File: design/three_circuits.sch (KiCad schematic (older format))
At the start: 0 parts

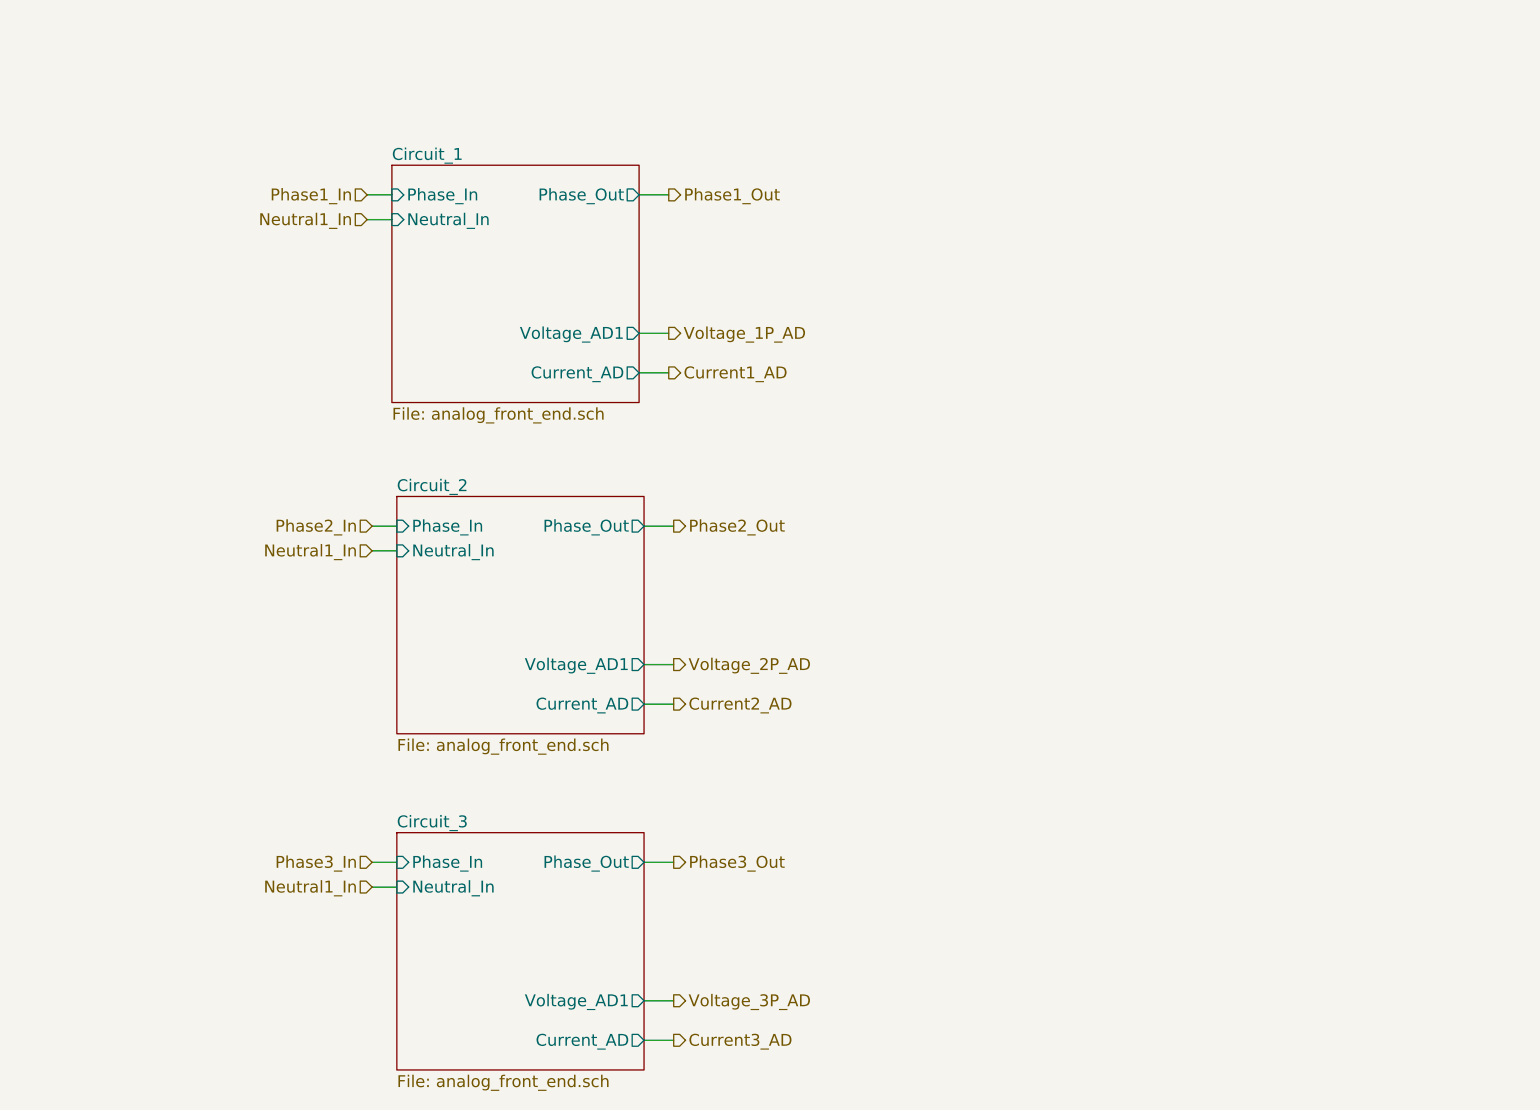
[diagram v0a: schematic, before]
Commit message: Moving to PIVI 2.0, added circuits for current clamps
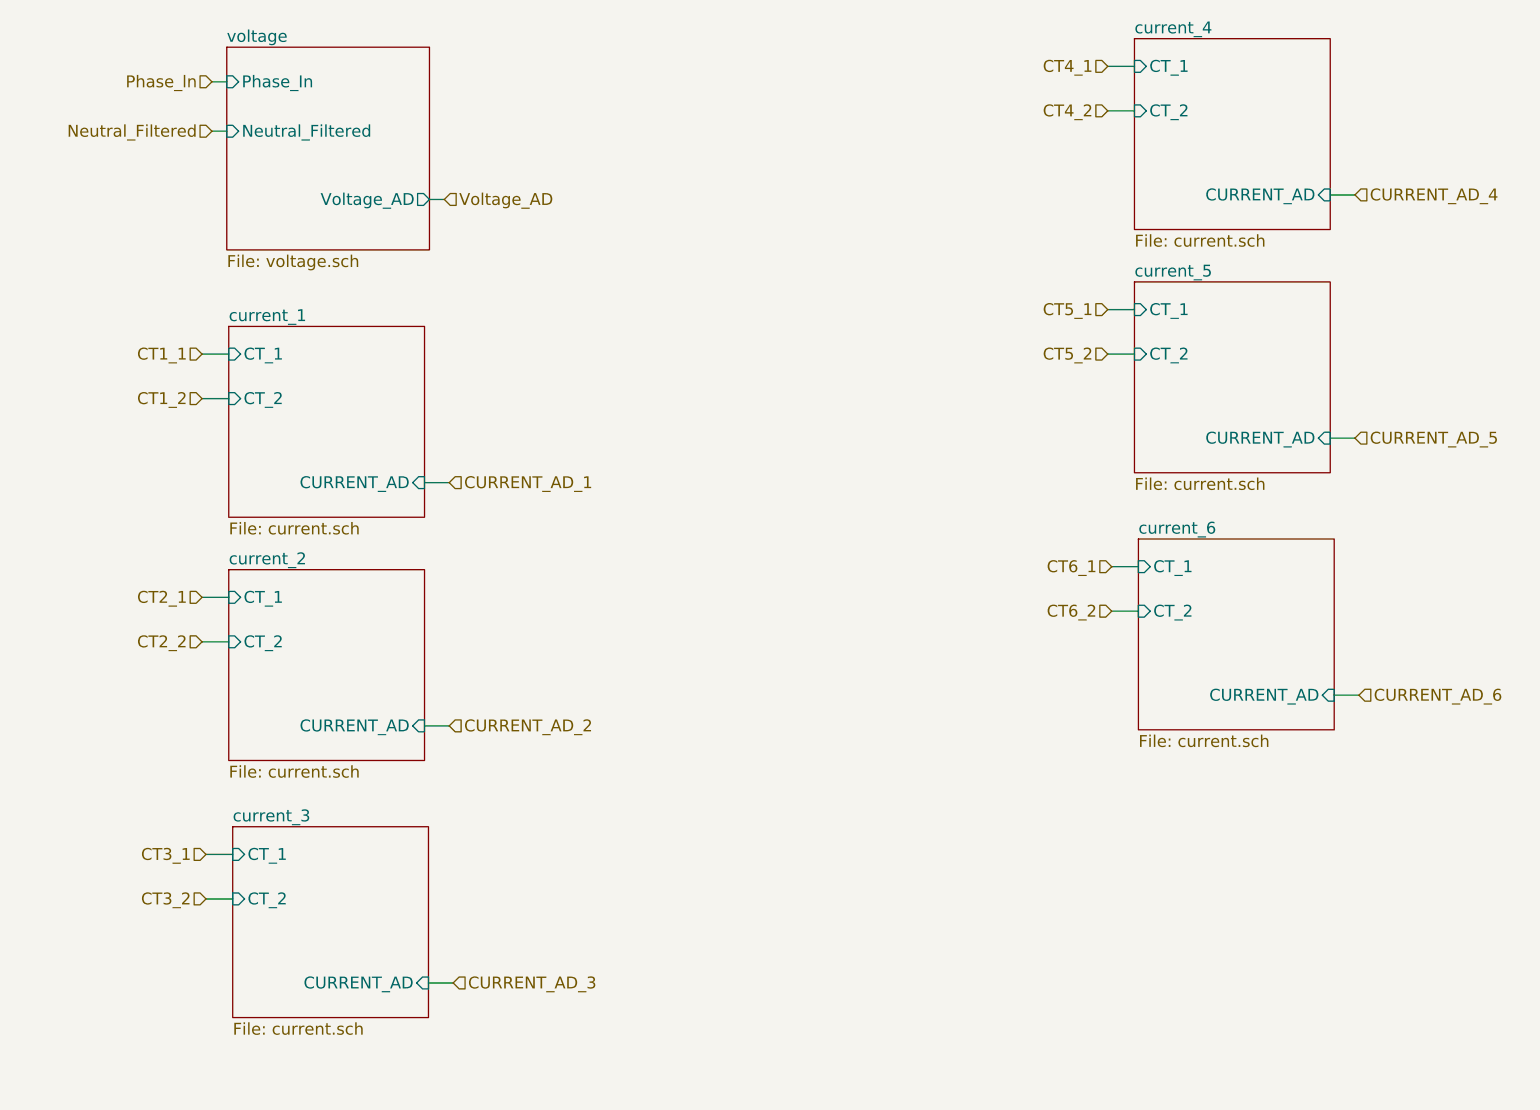
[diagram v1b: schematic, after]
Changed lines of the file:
@@
 LIBS:txs0104e
 LIBS:less
+LIBS:pivi-shield-cache
 EELAYER 25 0
 EELAYER END
 $Descr A4 11693 8268
 encoding utf-8
-Sheet 4 12
+Sheet 11 18
 Title "PIVI"
-Date ""
-Rev "1.0"
+Date "Mon 27 Jul 2015"
+Rev "2.0"
 Comp "Copyright (C) LESS industries S.A. 2014,2015"
 Comment1 "Share alike attribution non-commercial 4.0"
@@
 $EndDescr
 $Sheet
-S 2600 1500 1250 1200
-U 548E1940
-F0 "Circuit_1" 60
-F1 "analog_front_end.sch" 60
-F2 "Voltage_AD1" O R 3850 2350 60
-F3 "Phase_In" I L 2600 1650 60
-F4 "Phase_Out" O R 3850 1650 60
-F5 "Current_AD" O R 3850 2550 60
-F6 "Neutral_In" I L 2600 1775 60
+S 1765 903  1025 1025
+U 55B216B6
+F0 "voltage" 60
+F1 "voltage.sch" 60
+F2 "Phase_In" I L 1765 1078 60
+F3 "Voltage_AD" O R 2790 1673 60
+F4 "Neutral_Filtered" I L 1765 1328 60
 $EndSheet
+$Sheet
+S 1775 2315 990  965
+U 55B266EE
+F0 "current_1" 60
+F1 "current.sch" 60
+F2 "CT_1" I L 1775 2455 60
+F3 "CT_2" I L 1775 2680 60
+F4 "CURRENT_AD" I R 2765 3105 60
+$EndSheet
+Text HLabel 1690 1078 0    60   Input ~ 0
+Phase_ln
+Text HLabel 1640 2455 0    60   Input ~ 0
+CT1_1
+Text HLabel 1640 2680 0    60   Input ~ 0
+CT1_2
+Text HLabel 2890 3105 2    60   Input ~ 0
+CURRENT_AD_1
+$Sheet
+S 1775 3545 990  965
+U 55B3A3F6
+F0 "current_2" 60
+F1 "current.sch" 60
+F2 "CT_1" I L 1775 3685 60
+F3 "CT_2" I L 1775 3910 60
+F4 "CURRENT_AD" I R 2765 4335 60
+$EndSheet
+Text HLabel 1640 3685 0    60   Input ~ 0
+CT2_1
+Text HLabel 1640 3910 0    60   Input ~ 0
+CT2_2
+Text HLabel 2890 4335 2    60   Input ~ 0
+CURRENT_AD_2
+$Sheet
+S 1795 4845 990  965
+U 55B3A74F
+F0 "current_3" 60
+F1 "current.sch" 60
+F2 "CT_1" I L 1795 4985 60
+F3 "CT_2" I L 1795 5210 60
+F4 "CURRENT_AD" I R 2785 5635 60
+$EndSheet
+Text HLabel 1660 4985 0    60   Input ~ 0
+CT3_1
+Text HLabel 1660 5210 0    60   Input ~ 0
+CT3_2
+Text HLabel 2910 5635 2    60   Input ~ 0
+CURRENT_AD_3
+$Sheet
+S 6355 860  990  965
+U 55B3BD6E
+F0 "current_4" 60
+F1 "current.sch" 60
+F2 "CT_1" I L 6355 1000 60
+F3 "CT_2" I L 6355 1225 60
+F4 "CURRENT_AD" I R 7345 1650 60
+$EndSheet
+Text HLabel 6220 1000 0    60   Input ~ 0
+CT4_1
+Text HLabel 6220 1225 0    60   Input ~ 0
+CT4_2
+Text HLabel 7470 1650 2    60   Input ~ 0
+CURRENT_AD_4
+$Sheet
+S 6355 2090 990  965
+U 55B3BD79
+F0 "current_5" 60
+F1 "current.sch" 60
+F2 "CT_1" I L 6355 2230 60
+F3 "CT_2" I L 6355 2455 60
+F4 "CURRENT_AD" I R 7345 2880 60
+$EndSheet
+Text HLabel 6220 2230 0    60   Input ~ 0
+CT5_1
+Text HLabel 6220 2455 0    60   Input ~ 0
+CT5_2
+Text HLabel 7470 2880 2    60   Input ~ 0
+CURRENT_AD_5
+$Sheet
+S 6375 3390 990  965
+U 55B3BD84
+F0 "current_6" 60
+F1 "current.sch" 60
+F2 "CT_1" I L 6375 3530 60
+F3 "CT_2" I L 6375 3755 60
+F4 "CURRENT_AD" I R 7365 4180 60
+$EndSheet
+Text HLabel 6240 3530 0    60   Input ~ 0
+CT6_1
+Text HLabel 6240 3755 0    60   Input ~ 0
+CT6_2
+Text HLabel 7490 4180 2    60   Input ~ 0
+CURRENT_AD_6
+Text HLabel 2865 1673 2    60   Input ~ 0
+Voltage_AD
 Wire Wire Line
-	3850 1650 4000 1650
+	1690 1078 1765 1078
 Wire Wire Line
-	3850 2350 4000 2350
+	1690 1328 1765 1328
 Wire Wire Line
-	3850 2550 4000 2550
+	1775 2455 1640 2455
 Wire Wire Line
-	2600 1650 2475 1650
+	1640 2680 1775 2680
 Wire Wire Line
-	2600 1775 2475 1775
-Text HLabel 2475 1650 0    60   Input ~ 0
-Phase1_In
-Text HLabel 2475 1775 0    60   Input ~ 0
-Neutral1_In
-Text HLabel 4000 1650 2    60   Output ~ 0
-Phase1_Out
-Text HLabel 4000 2350 2    60   Output ~ 0
-Voltage_1P_AD
-Text HLabel 4000 2550 2    60   Output ~ 0
-Current1_AD
-$Sheet
-S 2625 3175 1250 1200
-U 548E244E
-F0 "Circuit_2" 60
-F1 "analog_front_end.sch" 60
-F2 "Voltage_AD1" O R 3875 4025 60
-F3 "Phase_In" I L 2625 3325 60
-F4 "Phase_Out" O R 3875 3325 60
-F5 "Current_AD" O R 3875 4225 60
-F6 "Neutral_In" I L 2625 3450 60
-$EndSheet
+	2765 3105 2890 3105
 Wire Wire Line
-	3875 3325 4025 3325
+	1775 3685 1640 3685
 Wire Wire Line
-	3875 4025 4025 4025
+	1640 3910 1775 3910
 Wire Wire Line
-	3875 4225 4025 4225
+	2765 4335 2890 4335
 Wire Wire Line
-	2625 3325 2500 3325
+	1795 4985 1660 4985
 Wire Wire Line
-	2625 3450 2500 3450
-Text HLabel 2500 3325 0    60   Input ~ 0
-Phase2_In
-Text HLabel 2500 3450 0    60   Input ~ 0
-Neutral1_In
-Text HLabel 4025 3325 2    60   Output ~ 0
-Phase2_Out
-Text HLabel 4025 4025 2    60   Output ~ 0
-Voltage_2P_AD
-Text HLabel 4025 4225 2    60   Output ~ 0
-Current2_AD
+	1660 5210 1795 5210
 Wire Wire Line
-	3875 5025 4025 5025
+	2785 5635 2910 5635
 Wire Wire Line
-	3875 5725 4025 5725
+	6355 1000 6220 1000
 Wire Wire Line
-	3875 5925 4025 5925
+	6220 1225 6355 1225
 Wire Wire Line
-	2625 5025 2500 5025
+	7345 1650 7470 1650
 Wire Wire Line
-	2625 5150 2500 5150
-Text HLabel 2500 5025 0    60   Input ~ 0
-Phase3_In
-Text HLabel 2500 5150 0    60   Input ~ 0
-Neutral1_In
-Text HLabel 4025 5025 2    60   Output ~ 0
-Phase3_Out
-Text HLabel 4025 5725 2    60   Output ~ 0
-Voltage_3P_AD
-Text HLabel 4025 5925 2    60   Output ~ 0
-Current3_AD
-$Sheet
-S 2625 4875 1250 1200
-U 548E282E
-F0 "Circuit_3" 60
-F1 "analog_front_end.sch" 60
-F2 "Voltage_AD1" O R 3875 5725 60
-F3 "Phase_In" I L 2625 5025 60
-F4 "Phase_Out" O R 3875 5025 60
-F5 "Current_AD" O R 3875 5925 60
-F6 "Neutral_In" I L 2625 5150 60
-$EndSheet
+	6355 2230 6220 2230
+Wire Wire Line
+	6220 2455 6355 2455
+Wire Wire Line
+	7345 2880 7470 2880
+Wire Wire Line
+	6375 3530 6240 3530
+Wire Wire Line
+	6240 3755 6375 3755
+Wire Wire Line
+	7365 4180 7490 4180
+Wire Wire Line
+	2790 1673 2865 1673
+Text HLabel 1690 1328 0    60   Input ~ 0
+Neutral_Filtered
 $EndSCHEMATC
